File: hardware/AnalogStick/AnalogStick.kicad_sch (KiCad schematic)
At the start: 2 parts, among them J1 Conn_01x06

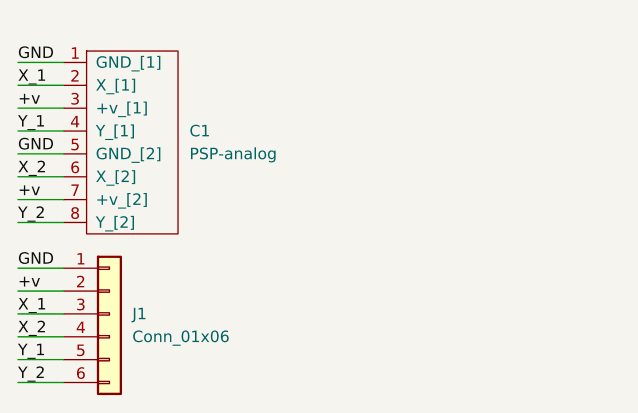
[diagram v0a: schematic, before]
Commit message: First pass analog stick FPC
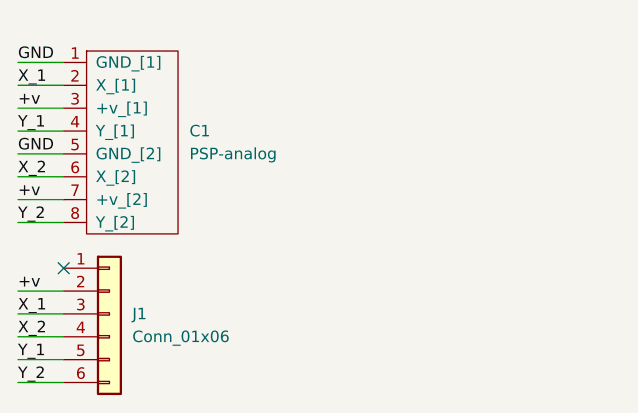
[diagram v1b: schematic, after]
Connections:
- net GND: no longer J1.1 (Pin_1)
- no-connect marks 0 -> 1
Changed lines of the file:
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@@
 (kicad_sch (version 20211123) (generator eeschema)
   (paper "A4")
+  (no_connect (at 82.55 68.58))
   (wire (pts (xy 77.47 71.12) (xy 82.55 71.12))
     (stroke (width 0) (type default) (color 0 0 0 0))
@@
   )
   (wire (pts (xy 77.47 58.42) (xy 82.55 58.42))
-    (stroke (width 0) (type default) (color 0 0 0 0))
-  )
-  (wire (pts (xy 77.47 68.58) (xy 82.55 68.58))
     (stroke (width 0) (type default) (color 0 0 0 0))
   )
@@
     (effects (font (size 1.27 1.27)) (justify left bottom))
   )
-  (label "GND" (at 77.47 68.58 0)
-    (effects (font (size 1.27 1.27)) (justify left bottom))
-  )

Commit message: Cleanup and add documentation
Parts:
- removed J1: Conn_01x06, Connector_FFC-FPC:Hirose_FH12-6S-0.5SH_1x06-1MP_P0.50mm_Horizontal, symbol Connector_Generic:Conn_01x06
- added TP1, TP2, TP3, TP4, TP5: TestPoint, TestPoint:TestPoint_Pad_1.0x1.0mm, symbol Connector:TestPoint
- C1: footprint trill-flex:PSP-analog -> consolizer:PSP-analog
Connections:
- net +v: now also TP1.1
- net X_1: now also TP2.1
- net X_2: now also TP3.1
- net Y_1: now also TP4.1
- net Y_2: now also TP5.1
- no-connect marks 1 -> 0
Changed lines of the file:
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@@
 (kicad_sch (version 20211123) (generator eeschema)
   (paper "A4")
-  (no_connect (at 82.55 68.58))
-  (wire (pts (xy 77.47 71.12) (xy 82.55 71.12))
-    (stroke (width 0) (type default) (color 0 0 0 0))
-  )
   (wire (pts (xy 77.47 60.96) (xy 82.55 60.96))
     (stroke (width 0) (type default) (color 0 0 0 0))
@@
     (stroke (width 0) (type default) (color 0 0 0 0))
   )
-  (wire (pts (xy 77.47 76.2) (xy 82.55 76.2))
-    (stroke (width 0) (type default) (color 0 0 0 0))
-  )
-  (wire (pts (xy 77.47 78.74) (xy 82.55 78.74))
-    (stroke (width 0) (type default) (color 0 0 0 0))
-  )
   (wire (pts (xy 77.47 50.8) (xy 82.55 50.8))
     (stroke (width 0) (type default) (color 0 0 0 0))
@@
     (stroke (width 0) (type default) (color 0 0 0 0))
   )
+  (wire (pts (xy 115.57 68.58) (xy 120.65 68.58))
+    (stroke (width 0) (type default) (color 0 0 0 0))
+  )
+  (wire (pts (xy 115.57 62.23) (xy 120.65 62.23))
+    (stroke (width 0) (type default) (color 0 0 0 0))
+  )
   (wire (pts (xy 77.47 55.88) (xy 82.55 55.88))
     (stroke (width 0) (type default) (color 0 0 0 0))
@@
     (stroke (width 0) (type default) (color 0 0 0 0))
   )
-  (wire (pts (xy 77.47 81.28) (xy 82.55 81.28))
+  (wire (pts (xy 115.57 73.66) (xy 120.65 73.66))
+    (stroke (width 0) (type default) (color 0 0 0 0))
+  )
+  (wire (pts (xy 115.57 52.07) (xy 120.65 52.07))
     (stroke (width 0) (type default) (color 0 0 0 0))
   )
@@
     (stroke (width 0) (type default) (color 0 0 0 0))
   )
-  (wire (pts (xy 77.47 73.66) (xy 82.55 73.66))
+  (wire (pts (xy 115.57 57.15) (xy 120.65 57.15))
     (stroke (width 0) (type default) (color 0 0 0 0))
   )
@@
     (stroke (width 0) (type default) (color 0 0 0 0))
   )
+  (label "X_2" (at 115.57 62.23 0)
+    (effects (font (size 1.27 1.27)) (justify left bottom))
+  )
+  (label "Y_1" (at 115.57 68.58 0)
+    (effects (font (size 1.27 1.27)) (justify left bottom))
+  )
   (label "X_1" (at 77.47 48.26 0)
     (effects (font (size 1.27 1.27)) (justify left bottom))
   )
-  (label "X_1" (at 77.47 73.66 0)
-    (effects (font (size 1.27 1.27)) (justify left bottom))
-  )
-  (label "Y_2" (at 77.47 81.28 0)
-    (effects (font (size 1.27 1.27)) (justify left bottom))
-  )
-  (label "X_2" (at 77.47 76.2 0)
+  (label "+v" (at 115.57 52.07 0)
     (effects (font (size 1.27 1.27)) (justify left bottom))
   )
@@
     (effects (font (size 1.27 1.27)) (justify left bottom))
   )
-  (label "Y_1" (at 77.47 78.74 0)
-    (effects (font (size 1.27 1.27)) (justify left bottom))
-  )
   (label "GND" (at 77.47 55.88 0)
     (effects (font (size 1.27 1.27)) (justify left bottom))
   )
-  (label "+v" (at 77.47 71.12 0)
-    (effects (font (size 1.27 1.27)) (justify left bottom))
-  )
   (label "+v" (at 77.47 50.8 0)
     (effects (font (size 1.27 1.27)) (justify left bottom))
@@
     (effects (font (size 1.27 1.27)) (justify left bottom))
   )
+  (label "Y_2" (at 115.57 73.66 0)
+    (effects (font (size 1.27 1.27)) (justify left bottom))
+  )
+  (label "X_1" (at 115.57 57.15 0)
+    (effects (font (size 1.27 1.27)) (justify left bottom))
+  )
+  (symbol (lib_id "Connector:TestPoint") (at 120.65 68.58 270) (unit 1)
+    (in_bom yes) (on_board yes) (fields_autoplaced)
+    (property "Reference" "TP4" (id 0) (at 125.73 67.3099 90)
+      (effects (font (size 1.27 1.27)) (justify left))
+    )
+    (property "Value" "TestPoint" (id 1) (at 125.73 69.8499 90)
+      (effects (font (size 1.27 1.27)) (justify left))
+    )
+    (property "Footprint" "TestPoint:TestPoint_Pad_1.0x1.0mm" (id 2) (at 120.65 73.66 0)
+      (effects (font (size 1.27 1.27)) hide)
+    )
+    (property "Datasheet" "~" (id 3) (at 120.65 73.66 0)
+      (effects (font (size 1.27 1.27)) hide)
+    )
+    (pin "1")
+  )
   (symbol (lib_id "consolizer:PSP-analog") (at 87.63 41.91 0) (unit 1)
     (in_bom yes) (on_board yes) (fields_autoplaced)
@@
       (effects (font (size 1.27 1.27)) (justify left))
     )
-    (property "Footprint" "trill-flex:PSP-analog" (id 2) (at 87.63 41.91 0)
+    (property "Footprint" "consolizer:PSP-analog" (id 2) (at 87.63 41.91 0)
       (effects (font (size 1.27 1.27)) hide)
     )
@@
     (pin "8")
   )
-  (symbol (lib_id "Connector_Generic:Conn_01x06") (at 87.63 73.66 0) (unit 1)
-    (in_bom yes) (on_board yes) (fields_autoplaced)
-    (property "Reference" "J1" (id 0) (at 90.17 73.6599 0)
-      (effects (font (size 1.27 1.27)) (justify left))
-    )
-    (property "Value" "Conn_01x06" (id 1) (at 90.17 76.1999 0)
-      (effects (font (size 1.27 1.27)) (justify left))
-    )
-    (property "Footprint" "Connector_FFC-FPC:Hirose_FH12-6S-0.5SH_1x06-1MP_P0.50mm_Horizontal" (id 2) (at 87.63 73.66 0)
-      (effects (font (size 1.27 1.27)) hide)
-    )
-    (property "Datasheet" "~" (id 3) (at 87.63 73.66 0)
-      (effects (font (size 1.27 1.27)) hide)
-    )
-    (pin "1")
-    (pin "2")
-    (pin "3")
-    (pin "4")
-    (pin "5")
-    (pin "6")
+  (symbol (lib_id "Connector:TestPoint") (at 120.65 62.23 270) (unit 1)
+    (in_bom yes) (on_board yes) (fields_autoplaced)
+    (property "Reference" "TP3" (id 0) (at 125.73 60.9599 90)
+      (effects (font (size 1.27 1.27)) (justify left))
+    )
+    (property "Value" "TestPoint" (id 1) (at 125.73 63.4999 90)
+      (effects (font (size 1.27 1.27)) (justify left))
+    )
+    (property "Footprint" "TestPoint:TestPoint_Pad_1.0x1.0mm" (id 2) (at 120.65 67.31 0)
+      (effects (font (size 1.27 1.27)) hide)
+    )
+    (property "Datasheet" "~" (id 3) (at 120.65 67.31 0)
+      (effects (font (size 1.27 1.27)) hide)
+    )
+    (pin "1")
+  )
+  (symbol (lib_id "Connector:TestPoint") (at 120.65 73.66 270) (unit 1)
+    (in_bom yes) (on_board yes) (fields_autoplaced)
+    (property "Reference" "TP5" (id 0) (at 125.73 72.3899 90)
+      (effects (font (size 1.27 1.27)) (justify left))
+    )
+    (property "Value" "TestPoint" (id 1) (at 125.73 74.9299 90)
+      (effects (font (size 1.27 1.27)) (justify left))
+    )
+    (property "Footprint" "TestPoint:TestPoint_Pad_1.0x1.0mm" (id 2) (at 120.65 78.74 0)
+      (effects (font (size 1.27 1.27)) hide)
+    )
+    (property "Datasheet" "~" (id 3) (at 120.65 78.74 0)
+      (effects (font (size 1.27 1.27)) hide)
+    )
+    (pin "1")
+  )
+  (symbol (lib_id "Connector:TestPoint") (at 120.65 52.07 270) (unit 1)
+    (in_bom yes) (on_board yes) (fields_autoplaced)
+    (property "Reference" "TP1" (id 0) (at 125.73 50.7999 90)
+      (effects (font (size 1.27 1.27)) (justify left))
+    )
+    (property "Value" "TestPoint" (id 1) (at 125.73 53.3399 90)
+      (effects (font (size 1.27 1.27)) (justify left))
+    )
+    (property "Footprint" "TestPoint:TestPoint_Pad_1.0x1.0mm" (id 2) (at 120.65 57.15 0)
+      (effects (font (size 1.27 1.27)) hide)
+    )
+    (property "Datasheet" "~" (id 3) (at 120.65 57.15 0)
+      (effects (font (size 1.27 1.27)) hide)
+    )
+    (pin "1")
+  )
+  (symbol (lib_id "Connector:TestPoint") (at 120.65 57.15 270) (unit 1)
+    (in_bom yes) (on_board yes) (fields_autoplaced)
+    (property "Reference" "TP2" (id 0) (at 125.73 55.8799 90)
+      (effects (font (size 1.27 1.27)) (justify left))
+    )
+    (property "Value" "TestPoint" (id 1) (at 125.73 58.4199 90)
+      (effects (font (size 1.27 1.27)) (justify left))
+    )
+    (property "Footprint" "TestPoint:TestPoint_Pad_1.0x1.0mm" (id 2) (at 120.65 62.23 0)
+      (effects (font (size 1.27 1.27)) hide)
+    )
+    (property "Datasheet" "~" (id 3) (at 120.65 62.23 0)
+      (effects (font (size 1.27 1.27)) hide)
+    )
+    (pin "1")
   )
   (sheet_instances
@@
   (symbol_instances
     (path "/5c1d6842-15a5-4f73-b198-8836681840a1"
-      (reference "C1") (unit 1) (value "PSP-analog") (footprint "trill-flex:PSP-analog")
-    )
-    (path "/dd3da890-32ef-4a5a-aea4-e5d2141f1ff1"
-      (reference "J1") (unit 1) (value "Conn_01x06") (footprint "Connector_FFC-FPC:Hirose_FH12-6S-0.5SH_1x06-1MP_P0.50mm_Horizontal")
-    )
-  )
+      (reference "C1") (unit 1) (value "PSP-analog") (footprint "consolizer:PSP-analog")
+    )
+    (path "/e4a4d2c2-5110-48ca-964d-53828b9da081"
+      (reference "TP1") (unit 1) (value "TestPoint") (footprint "TestPoint:TestPoint_Pad_1.0x1.0mm")
+    )
+    (path "/e80103aa-5561-41fe-a0b4-fba0004b739b"
+      (reference "TP2") (unit 1) (value "TestPoint") (footprint "TestPoint:TestPoint_Pad_1.0x1.0mm")
+    )
+    (path "/64b3d758-146d-498c-8e36-a7162573fa48"
+      (reference "TP3") (unit 1) (value "TestPoint") (footprint "TestPoint:TestPoint_Pad_1.0x1.0mm")
+    )
+    (path "/2ffab9c3-5c7a-4d55-af94-9f9bd8be80ab"
+      (reference "TP4") (unit 1) (value "TestPoint") (footprint "TestPoint:TestPoint_Pad_1.0x1.0mm")
+    )
+    (path "/ce3b7f99-7920-4450-9cce-f9c9b5b48a38"
+      (reference "TP5") (unit 1) (value "TestPoint") (footprint "TestPoint:TestPoint_Pad_1.0x1.0mm")
+    )
+  )

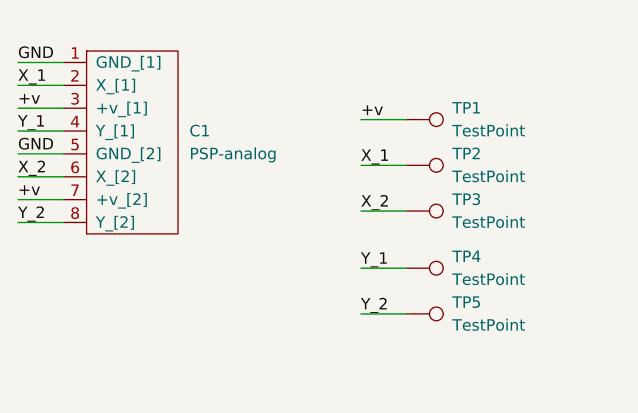
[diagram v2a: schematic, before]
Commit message: Added analog stick
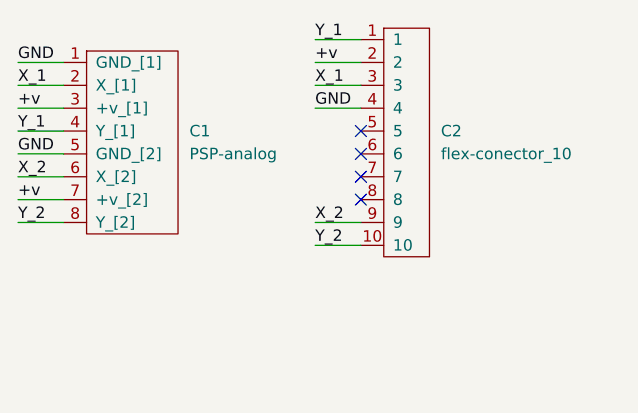
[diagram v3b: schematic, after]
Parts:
- removed TP1, TP2, TP3, TP4, TP5: TestPoint, TestPoint:TestPoint_Pad_1.0x1.0mm, symbol Connector:TestPoint
- added C2: flex-conector_10, consolizer:flex_long_10, symbol consolizer:flex-conector_10
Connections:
- net +v: now also C2.2
- net GND: now also C2.4
- net X_1: now also C2.3
- net X_2: now also C2.9
- net Y_1: now also C2.1
- net Y_2: now also C2.10
- no-connect marks 0 -> 4
